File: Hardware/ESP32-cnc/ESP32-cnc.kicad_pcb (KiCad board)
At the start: 2 copper layers, 85 parts, among them J1 Inputs, J10 Y-Servo, J11 X_STEP_B, J12 Y_STEP_B, J13 Spindle On/Off, J14 X_STEP_A, J15 Y_STEP_A, J16 Z_STEP, J2 12-18V DC, J3 Conn_01x19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

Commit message: minor updates
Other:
- board outline added: 100 x 100 mm
- board text added: "+5V"
- board text added: "EPS32-GRBL-CNC"
- board text added: "GND"
- board text added: "ILCK"
- board text added: "PWM"
- board text added: "SPINDLE 5V PWM"
- board text removed: "INTERLOCK"
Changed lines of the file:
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@@
   (general
     (thickness 1.6)
-    (drawings 26)
+    (drawings 39)
     (tracks 724)
     (zones 0)
@@
     (31 B.Cu signal)
     (32 B.Adhes user)
-    (33 F.Adhes user hide)
+    (33 F.Adhes user)
     (34 B.Paste user)
     (35 F.Paste user)
@@
     (38 B.Mask user)
     (39 F.Mask user)
-    (40 Dwgs.User user hide)
-    (41 Cmts.User user hide)
-    (42 Eco1.User user hide)
-    (43 Eco2.User user hide)
+    (40 Dwgs.User user)
+    (41 Cmts.User user)
+    (42 Eco1.User user)
+    (43 Eco2.User user)
     (44 Edge.Cuts user)
     (45 Margin user)
@@
     (descr "Through hole straight pin header, 2x05, 2.54mm pitch, double rows")
     (tags "Through hole pin header THT 2x05 2.54mm double row")
-    (fp_text reference J7 (at 1.27 -2.33) (layer F.SilkS)
+    (fp_text reference J7 (at 2.9845 -2.6035) (layer F.SilkS)
       (effects (font (size 1 1) (thickness 0.15)))
     )
@@
     (tags SOT-23)
     (attr smd)
-    (fp_text reference Q1 (at 0 -2.5 90) (layer F.SilkS)
+    (fp_text reference Q1 (at -2.511 0.035 180) (layer F.SilkS)
       (effects (font (size 1 1) (thickness 0.15)))
     )
@@
       (net 2 GND))
   )
+  (gr_text GND (at 103.505 87.884 90) (layer F.SilkS)
+    (effects (font (size 1 1) (thickness 0.15)))
+  )
+  (gr_text PWM (at 101.0285 87.884 90) (layer F.SilkS)
+    (effects (font (size 1 1) (thickness 0.15)))
+  )
+  (gr_text ILCK (at 97.028 88.773) (layer F.SilkS)
+    (effects (font (size 1 1) (thickness 0.15)))
+  )
+  (gr_text GND (at 105.4735 83.312 90) (layer F.SilkS)
+    (effects (font (size 1 1) (thickness 0.15)))
+  )
+  (gr_text GND (at 107.315 48.26) (layer F.SilkS)
+    (effects (font (size 1 1) (thickness 0.15)))
+  )
+  (gr_text GND (at 107.315 53.213) (layer F.SilkS)
+    (effects (font (size 1 1) (thickness 0.15)))
+  )
+  (gr_text GND (at 107.315 58.3565) (layer F.SilkS)
+    (effects (font (size 1 1) (thickness 0.15)))
+  )
+  (gr_text "GND\n" (at 107.315 63.4365) (layer F.SilkS)
+    (effects (font (size 1 1) (thickness 0.15)))
+  )
+  (gr_text GND (at 105.664 66.4845 90) (layer F.SilkS)
+    (effects (font (size 1 1) (thickness 0.15)))
+  )
+  (gr_text +5V (at 73.4695 120.777 90) (layer F.SilkS)
+    (effects (font (size 1 1) (thickness 0.15)))
+  )
+  (gr_text GND (at 70.866 120.5865 90) (layer F.SilkS)
+    (effects (font (size 1 1) (thickness 0.15)))
+  )
+  (gr_text GND (at 51.689 132.08 90) (layer F.SilkS)
+    (effects (font (size 1 1) (thickness 0.15)))
+  )
+  (gr_text EPS32-GRBL-CNC (at 76.5175 129.032) (layer F.SilkS)
+    (effects (font (size 1 1) (thickness 0.25)))
+  )
   (gr_text "X-AXIS 2" (at 16.637 50.292 90) (layer F.SilkS)
     (effects (font (size 1 1) (thickness 0.15)))
@@
     (effects (font (size 1 1) (thickness 0.15)))
   )
-  (gr_text "PROBE\n" (at 108.2675 60.96) (layer F.SilkS)
+  (gr_text "PROBE\n" (at 108.267381 60.96) (layer F.SilkS)
     (effects (font (size 1 1) (thickness 0.15)))
   )
-  (gr_text RESET (at 108.0135 55.88) (layer F.SilkS)
+  (gr_text RESET (at 108.053096 55.88) (layer F.SilkS)
     (effects (font (size 1 1) (thickness 0.15)))
   )
-  (gr_text START (at 107.823 50.927) (layer F.SilkS)
+  (gr_text START (at 107.957857 50.927) (layer F.SilkS)
     (effects (font (size 1 1) (thickness 0.15)))
   )
-  (gr_text HOLD (at 107.3785 45.6565) (layer F.SilkS)
+  (gr_text HOLD (at 107.743572 45.6565) (layer F.SilkS)
     (effects (font (size 1 1) (thickness 0.15)))
   )
@@
     (effects (font (size 1 1) (thickness 0.15)))
   )
-  (gr_text "INTERLOCK\n" (at 98.8695 88.2015) (layer F.SilkS)
+  (gr_text "SPINDLE\n5V PWM" (at 108.331 90.7415 90) (layer F.SilkS)
     (effects (font (size 1 1) (thickness 0.15)))
   )
-  (gr_text X (at 108.5215 69.5325 90) (layer F.SilkS)
+  (gr_text X (at 108.458 69.5325 90) (layer F.SilkS)
     (effects (font (size 1 1) (thickness 0.15)))
   )
-  (gr_text X (at 108.5215 72.0725 90) (layer F.SilkS)
+  (gr_text X (at 108.458 72.0725 90) (layer F.SilkS)
     (effects (font (size 1 1) (thickness 0.15)))
   )
-  (gr_text Y (at 108.3945 74.676 90) (layer F.SilkS)
+  (gr_text Y (at 108.458 74.676 90) (layer F.SilkS)
     (effects (font (size 1 1) (thickness 0.15)))
   )
@@
     (effects (font (size 1 1) (thickness 0.15)) (justify mirror))
   )
-  (gr_line (start 115 135) (end 115 35) (layer F.SilkS) (width 0.12))
-  (gr_line (start 15 135) (end 115 135) (layer F.SilkS) (width 0.12))
-  (gr_line (start 15 35) (end 15 135) (layer F.SilkS) (width 0.12))
-  (gr_line (start 15 35) (end 115 35) (layer F.SilkS) (width 0.12))
+  (gr_line (start 115 135) (end 115 35) (layer Edge.Cuts) (width 0.12))
+  (gr_line (start 15 135) (end 115 135) (layer Edge.Cuts) (width 0.12))
+  (gr_line (start 15 35) (end 15 135) (layer Edge.Cuts) (width 0.12))
+  (gr_line (start 15 35) (end 115 35) (layer Edge.Cuts) (width 0.12))
   (segment (start 61 124.02) (end 57.7824 120.8024) (width 3) (layer F.Cu) (net 1))
   (segment (start 61 129) (end 61 124.02) (width 3) (layer F.Cu) (net 1))

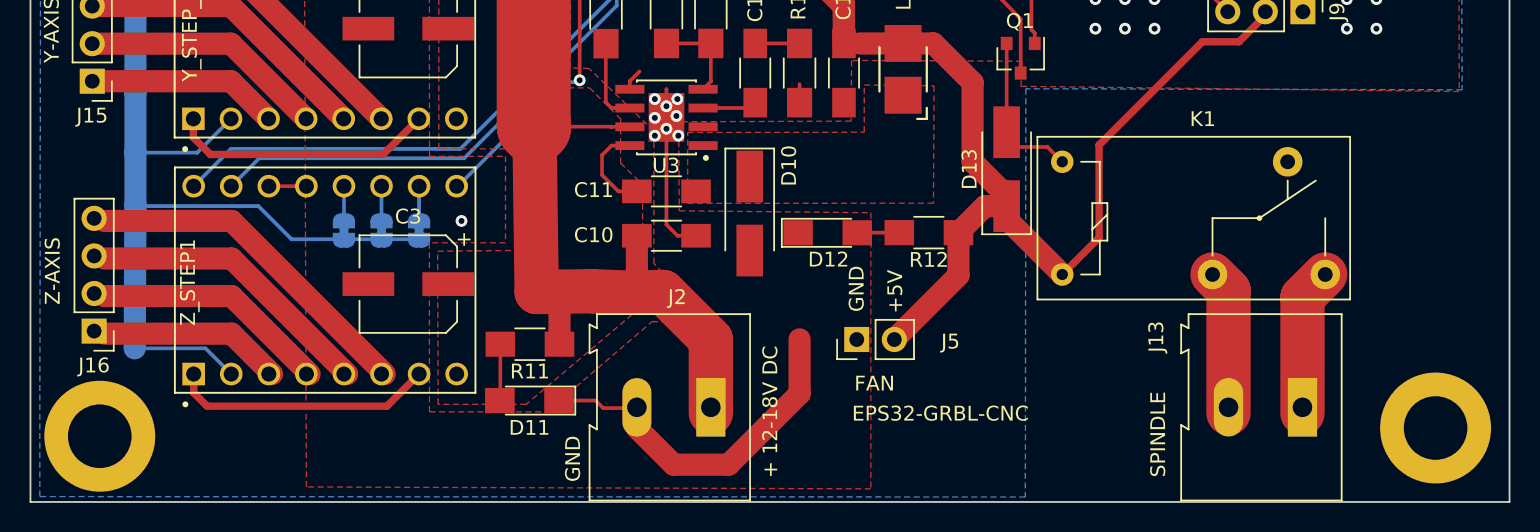
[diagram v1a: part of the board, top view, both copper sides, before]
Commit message: footprint adaption
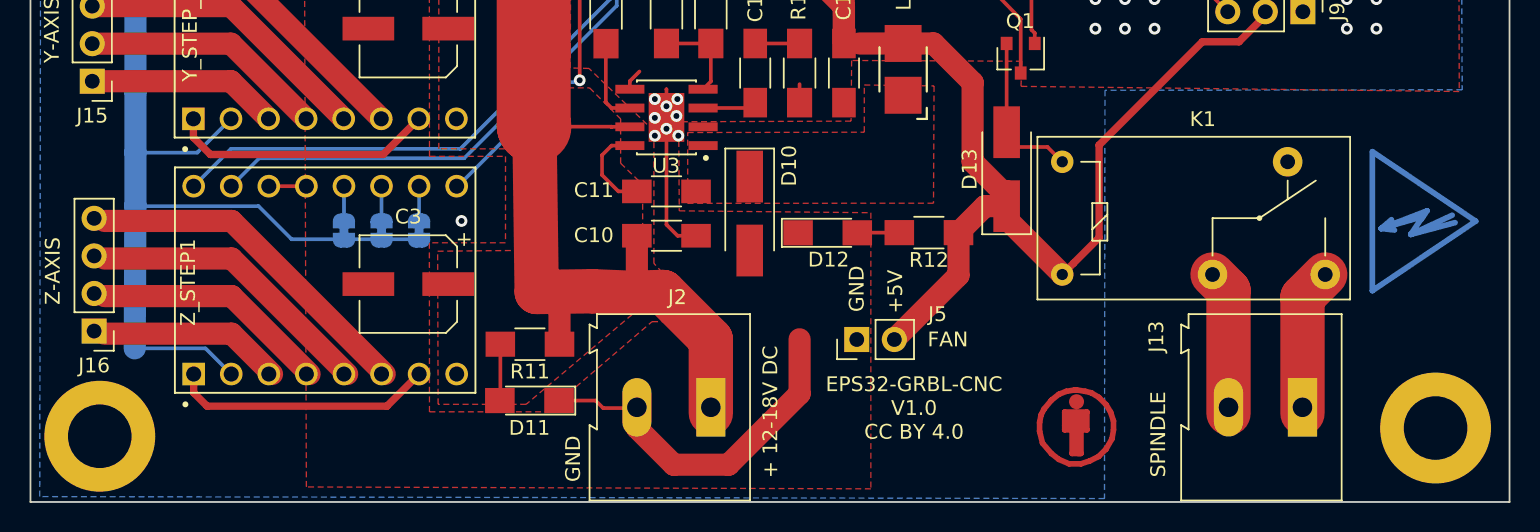
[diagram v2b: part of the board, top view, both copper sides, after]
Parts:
- added LOGO1: Logo_Open_Hardware_Large, Symbols:OSHW-Symbol_22.3x20mm_SilkScreen, B.Cu at (67.5, 109.0)
- added LOGO2: SYM_CC_BY, Symbols:Symbol_CreativeCommonsPublicDomain_SilkScreenTop_Small, B.Cu at (72.5, 71.6)
- added LOGO3: SYM_CC_BY, Symbols:Symbol_CC-Attribution_CopperTop_Small, F.Cu at (85.7, 129.9)
- added SYM1: SYM_Flash_Small, Symbols:Symbol_HighVoltage_Type2_CopperTop_VerySmall, B.Cu at (108.5, 116.0)
- Enable_Servos1: renamed from JP1; value SolderJumper_2_Bridged -> Enable_Servos
- J8: value Enable Spindle -> PWM Spindle (5V)
- X_MS1: value X2_MS1 -> X_MS1
- X_MS2: value X2_MS2 -> X_MS2
- X_MS3: value X2_MS3 -> X_MS3
- Y2_MS1: value X2_MS1 -> Y2_MS1
- Y2_MS2: value X2_MS2 -> Y2_MS2
- Y2_MS3: value X2_MS3 -> Y2_MS3
- Y_MS1: value X2_MS1 -> Y_MS1
- Y_MS2: value X2_MS2 -> Y_MS2
- Y_MS3: value X2_MS3 -> Y_MS3
- Z_MS1: value X2_MS1 -> Z_MS1
- Z_MS2: value X2_MS2 -> Z_MS2
- Z_MS3: value X2_MS3 -> Z_MS3
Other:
- board text added: "EPS32-GRBL-CNC V1.0 CC BY 4.0"
- board text removed: "EPS32-GRBL-CNC"
